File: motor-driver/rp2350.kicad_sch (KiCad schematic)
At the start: 0 parts

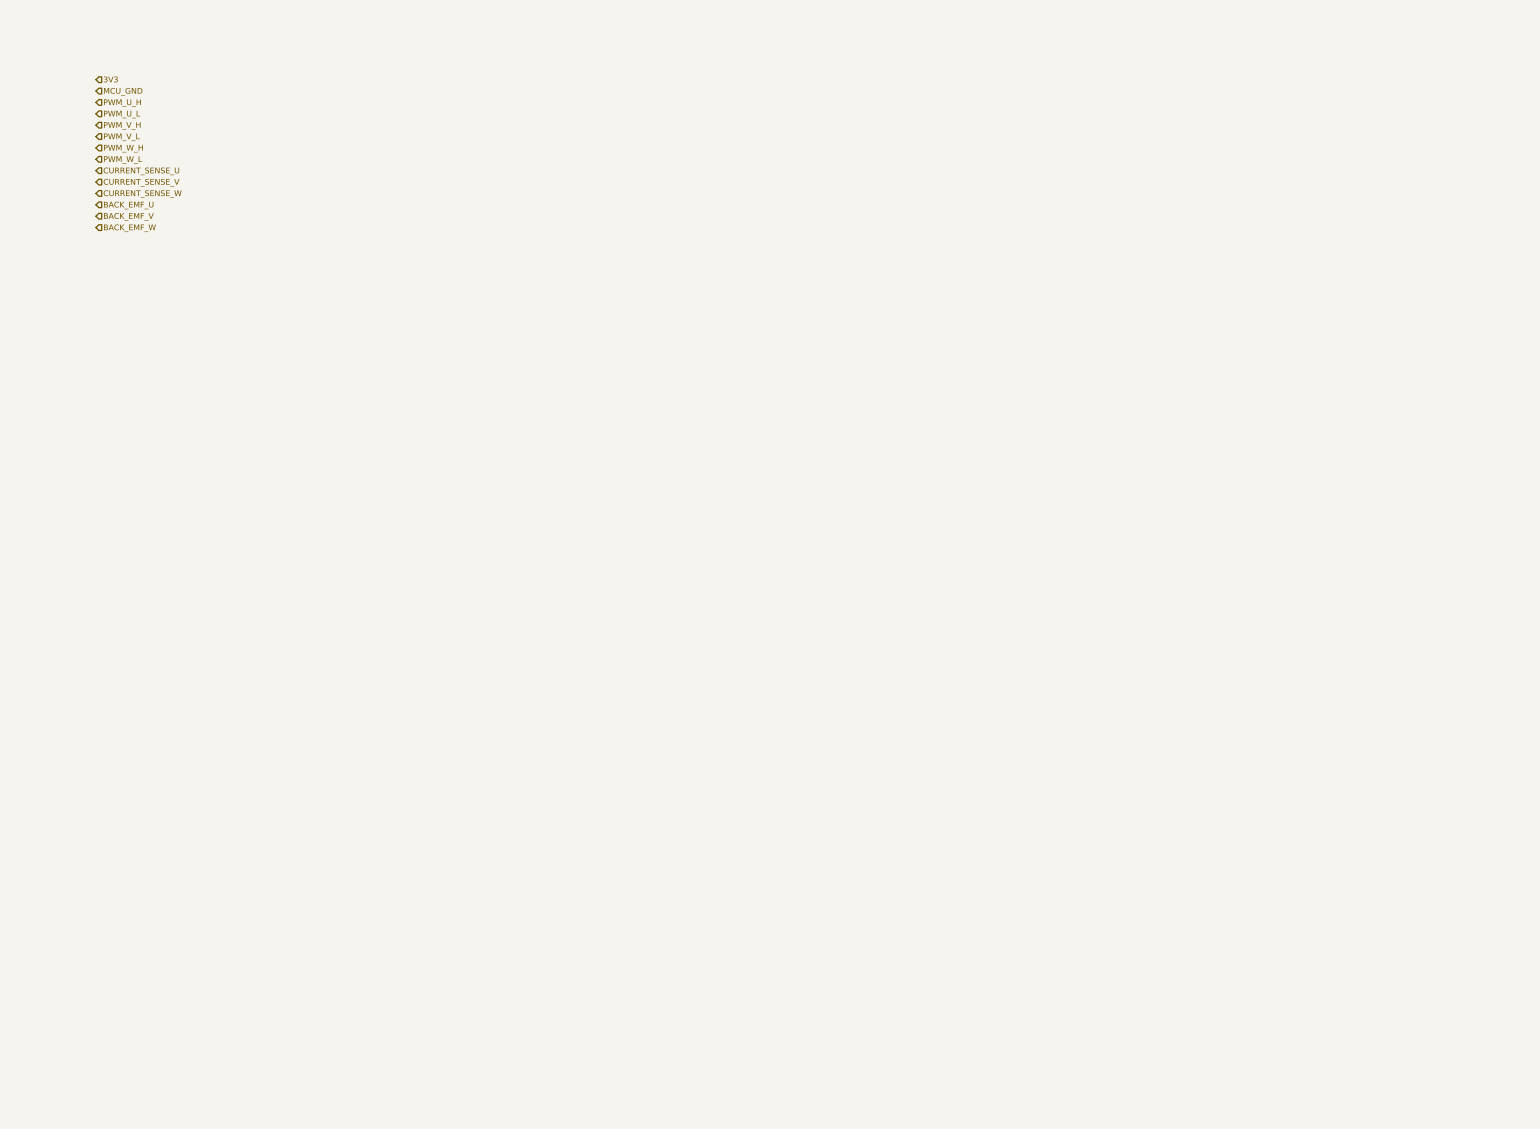
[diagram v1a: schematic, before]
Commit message: added connectors starting pcb layout
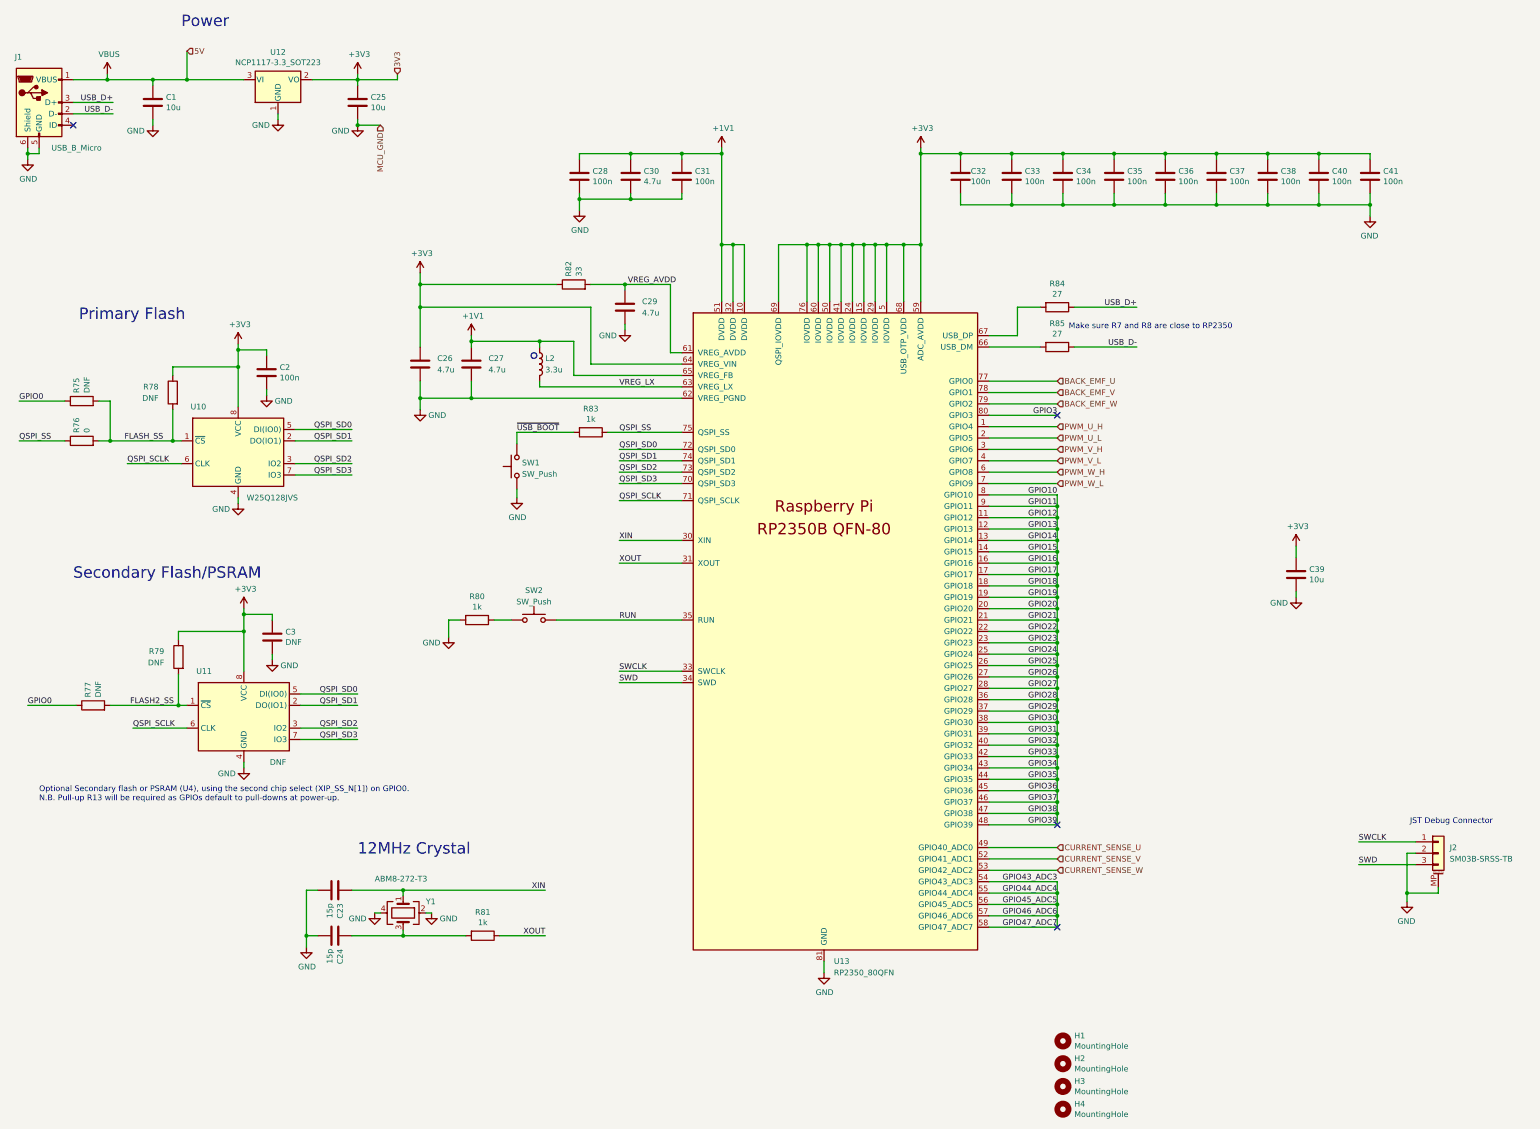
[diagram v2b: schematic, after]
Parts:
- added C1, C25, C39: 10u, Capacitor_SMD:C_0805_2012Metric, symbol Device:C
- added C2, C28, C31, C32, C33, C34, C35, C36, C37, C38, C40, C41: 100n, Capacitor_SMD:C_0402_1005Metric, symbol Device:C
- added C23, C24: 15p, Capacitor_SMD:C_0402_1005Metric, symbol Device:C
- added C26, C27: 4.7u, Capacitor_SMD:C_0603_1608Metric, symbol Device:C
- added C29, C30: 4.7u, Capacitor_SMD:C_0402_1005Metric, symbol Device:C
- added C3: DNF, Capacitor_SMD:C_0402_1005Metric, symbol Device:C
- added H1, H2, H3, H4: MountingHole, MountingHole:MountingHole_2.7mm_M2.5, symbol Mechanical:MountingHole
- added J1: USB_B_Micro, Connector_USB:USB_Micro-B_Amphenol_10103594-0001LF_Horizontal, symbol Connector:USB_B_Micro
- added J2: SM03B-SRSS-TB, Connector_JST:JST_SH_SM03B-SRSS-TB_1x03-1MP_P1.00mm_Horizontal, symbol Connector_Generic_MountingPin:Conn_01x03_MountingPin
- added L2: 3.3u, Inductor_SMD:L_0603_1608Metric, symbol Device:L
- added R75, R77, R78, R79: DNF, Resistor_SMD:R_0402_1005Metric, symbol Device:R
- added R76: 0, Resistor_SMD:R_0402_1005Metric, symbol Device:R
- added R80, R81, R83: 1k, Resistor_SMD:R_0402_1005Metric, symbol Device:R
- added R82: 33, Resistor_SMD:R_0402_1005Metric, symbol Device:R
- added R84, R85: 27, Resistor_SMD:R_0402_1005Metric, symbol Device:R
- added SW1, SW2: SW_Push, Button_Switch_SMD:SW_Push_1P1T_NO_Vertical_Wuerth_434133025816, symbol Switch:SW_Push
- added U10: W25Q128JVS, Package_SO_new:SOIC-8_5.23x5.23mm_P1.27mm, symbol Memory_Flash:W25Q128JVS
- added U11: DNF, Package_SO_new:SOIC-8_5.23x5.23mm_P1.27mm, symbol Memory_Flash:W25Q128JVS
- added U12: NCP1117-3.3_SOT223, Package_TO_SOT_SMD:SOT-223-3_TabPin2, symbol Regulator_Linear:NCP1117-3.3_SOT223
- added U13: RP2350_80QFN, RP2350_80QFN_minimal:RP2350-QFN-80-1EP_10x10_P0.4mm_EP3.4x3.4mm_ThermalVias, symbol MCU_RaspberryPi_RP2350:RP2350_80QFN
- added Y1: ABM8-272-T3, Crystal:Crystal_SMD_3225-4Pin_3.2x2.5mm, symbol Device:Crystal_GND24
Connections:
- net BACK_EMF_U: now also U13.77 (GPIO0)
- net BACK_EMF_V: now also U13.78 (GPIO1)
- net BACK_EMF_W: now also U13.79 (GPIO2)
- net CURRENT_SENSE_U: now also U13.49 (GPIO40_ADC0)
- net CURRENT_SENSE_V: now also U13.52 (GPIO41_ADC1)
- net CURRENT_SENSE_W: now also U13.53 (GPIO42_ADC2)
- net PWM_U_H: now also U13.1 (GPIO4)
- net PWM_U_L: now also U13.2 (GPIO5)
- net PWM_V_H: now also U13.3 (GPIO6)
- net PWM_V_L: now also U13.4 (GPIO7)
- net PWM_W_H: now also U13.6 (GPIO8)
- net PWM_W_L: now also U13.7 (GPIO9)
- new net: C24.1, R81.2, Y1.3
- new net: R84.2, U13.67 (USB_DP)
- new net: R85.2, U13.66 (USB_DM)
- new net: R80.1, SW2.1
- new net +1V1: C27.1, C28.1, C30.1, C31.1, L2.1, U13.10 (DVDD), U13.32 (DVDD), U13.51 (DVDD), U13.65 (VREG_FB)
- new net +3V3: C2.1, C25.1, C26.1, C3.1, C32.1, C33.1, C34.1, C35.1, C36.1, C37.1, C38.1, C39.1, C40.1, C41.1, R78.1, R79.1, R82.1, U10.8 (VCC), U11.8 (VCC), U12.2 (VO), U13.15 (IOVDD), U13.24 (IOVDD), U13.29 (IOVDD), U13.41 (IOVDD), U13.5 (IOVDD), U13.50 (IOVDD), U13.59 (ADC_AVDD), U13.60 (IOVDD), U13.64 (VREG_VIN), U13.68 (USB_OTP_VDD), U13.69 (QSPI_IOVDD), U13.76 (IOVDD)
- new net FLASH2_SS: R77.2, R79.2, U11.1 (~{CS})
- new net FLASH_SS: R75.2, R76.2, R78.2, U10.1 (~{CS})
- new net GND: C1.2, C2.2, C23.2, C24.2, C25.2, C26.2, C27.2, C28.2, C29.2, C3.2, C30.2, C31.2, C32.2, C33.2, C34.2, C35.2, C36.2, C37.2, C38.2, C39.2, C40.2, C41.2, J1.5 (GND), J1.6 (Shield), J2.2 (Pin_2), J2.MP (MountPin), R80.2, SW1.1, U10.4 (GND), U11.4 (GND), U12.1 (GND), U13.62 (VREG_PGND), U13.81 (GND), Y1.2, Y1.4
- new net GPIO0: R75.1, R77.1
- new net GPIO10: U13.11 (GPIO12), U13.12 (GPIO13), U13.13 (GPIO14), U13.14 (GPIO15), U13.16 (GPIO16), U13.17 (GPIO17), U13.18 (GPIO18), U13.19 (GPIO19), U13.20 (GPIO20), U13.21 (GPIO21), U13.22 (GPIO22), U13.23 (GPIO23), U13.25 (GPIO24), U13.26 (GPIO25), U13.27 (GPIO26), U13.28 (GPIO27), U13.36 (GPIO28), U13.37 (GPIO29), U13.38 (GPIO30), U13.39 (GPIO31), U13.40 (GPIO32), U13.42 (GPIO33), U13.43 (GPIO34), U13.44 (GPIO35), U13.45 (GPIO36), U13.46 (GPIO37), U13.47 (GPIO38), U13.48 (GPIO39), U13.8 (GPIO10), U13.9 (GPIO11)
- new net GPIO3: U13.80 (GPIO3)
- new net GPIO43_ADC3: U13.54 (GPIO43_ADC3), U13.55 (GPIO44_ADC4), U13.56 (GPIO45_ADC5), U13.57 (GPIO46_ADC6), U13.58 (GPIO47_ADC7)
- new net QSPI_SCLK: U10.6 (CLK), U11.6 (CLK), U13.71 (QSPI_SCLK)
- new net QSPI_SD0: U10.5 (DI(IO0)), U11.5 (DI(IO0)), U13.72 (QSPI_SD0)
- new net QSPI_SD1: U10.2 (DO(IO1)), U11.2 (DO(IO1)), U13.74 (QSPI_SD1)
- new net QSPI_SD2: U10.3 (IO2), U11.3 (IO2), U13.73 (QSPI_SD2)
- new net QSPI_SD3: U10.7 (IO3), U11.7 (IO3), U13.70 (QSPI_SD3)
- new net QSPI_SS: R76.1, R83.1, U13.75 (QSPI_SS)
- new net RUN: SW2.2, U13.35 (RUN)
- new net SWCLK: J2.1 (Pin_1), U13.33 (SWCLK)
- new net SWD: J2.3 (Pin_3), U13.34 (SWD)
- new net USB_D+: J1.3 (D+), R84.1
- new net USB_D-: J1.2 (D-), R85.1
- new net VBUS: C1.1, J1.1 (VBUS), U12.3 (VI)
- new net VREG_AVDD: C29.1, R82.2, U13.61 (VREG_AVDD)
- new net VREG_LX: L2.2, U13.63 (VREG_LX)
- new net XIN: C23.1, U13.30 (XIN), Y1.1
- new net XOUT: R81.1, U13.31 (XOUT)
- new net ~{USB_BOOT}: R83.2, SW1.2
- no-connect marks 0 -> 4
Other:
- note added: "12MHz Crystal"
- note added: "JST Debug Connector"
- note added: "Make sure R7 and R8 are close to RP2350"
- note added: "Optional Secondary flash or PSRAM (U4), using the second chip select (XIP_SS_N[1]) on GPIO0. N.B. Pull-up R13 will be required as GPIOs default to pull-downs at power-up."
- note added: "Power"
- note added: "Primary Flash"
- note added: "Secondary Flash/PSRAM"
- company: (none) -> Raspberry Pi Ltd
- title: (none) -> RP2350B QFN80 Minimal Design Example

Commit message: commit before changing custom sullen key sense
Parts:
- removed C1: 10u, Capacitor_SMD:C_0805_2012Metric, symbol Device:C
- C25, C39: footprint Capacitor_SMD:C_0805_2012Metric -> Capacitor_SMD:C_0603_1608Metric
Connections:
- net VBUS: no longer names the net of J1.1 (VBUS)
- net VBUS: no longer U12.3 (VI)
- new net 5V: U12.3 (VI)
- no-connect marks 4 -> 5

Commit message: post revisions
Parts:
- removed C3: DNF, Capacitor_SMD:C_0402_1005Metric, symbol Device:C
- removed J1: USB_B_Micro, Connector_USB:USB_Micro-B_Amphenol_10103594-0001LF_Horizontal, symbol Connector:USB_B_Micro
- removed R77, R79: DNF, Resistor_SMD:R_0402_1005Metric, symbol Device:R
- removed U11: DNF, Package_SO_new:SOIC-8_5.23x5.23mm_P1.27mm, symbol Memory_Flash:W25Q128JVS
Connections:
- no-connect marks 5 -> 3
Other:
- note removed: "Optional Secondary flash or PSRAM (U4), using the second chip select (XIP_SS_N[1]) on GPIO0. N.B. Pull-up R13 will be required as GPIOs default to pull-downs at power-up."
- note removed: "Secondary Flash/PSRAM"
- company: Raspberry Pi Ltd -> Drone 
